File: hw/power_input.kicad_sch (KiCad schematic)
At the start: 8 parts, among them J2 216990-0002, U4 USBLC6-2SC6, U5 TLV70233DSER

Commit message: WIP - nearly all routing complete
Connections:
- net USB_P: now reaches J2.A6 (DP1), J2.B6 (DP2), U4.4
- net USB_N: now reaches J2.A7 (DN1), J2.B7 (DN2), U4.6
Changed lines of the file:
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@@
     (stroke (width 0) (type default))
+  )
+  (label "USB_N" (at 128.27 102.87 0) (fields_autoplaced)
+    (effects (font (size 1.27 1.27)) (justify left bottom))
+  )
+  (label "USB_P" (at 124.46 128.27 0) (fields_autoplaced)
+    (effects (font (size 1.27 1.27)) (justify left bottom))
   )
   (global_label "+3V" (shape input) (at 173.99 54.61 90) (fields_autoplaced)
@@
     (effects (font (size 1.27 1.27)) (justify left))
   )
+  (netclass_flag "" (length 2.54) (shape round) (at 124.46 102.87 0) (fields_autoplaced)
+    (effects (font (size 1.27 1.27)) (justify left bottom))
+    (property "Netclass" "usb" (at 125.0696 100.33 0)
+      (effects (font (size 1.27 1.27) italic) (justify left))
+    )
+  )
+  (netclass_flag "" (length 2.54) (shape round) (at 191.77 113.03 0) (fields_autoplaced)
+    (effects (font (size 1.27 1.27)) (justify left bottom))
+    (property "Netclass" "usb" (at 192.3796 110.49 0)
+      (effects (font (size 1.27 1.27) italic) (justify left))
+    )
+  )
+  (netclass_flag "" (length 2.54) (shape round) (at 134.62 113.03 0) (fields_autoplaced)
+    (effects (font (size 1.27 1.27)) (justify left bottom))
+    (property "Netclass" "usb" (at 135.2296 110.49 0)
+      (effects (font (size 1.27 1.27) italic) (justify left))
+    )
+  )
+  (netclass_flag "" (length 2.54) (shape round) (at 191.77 102.87 0) (fields_autoplaced)
+    (effects (font (size 1.27 1.27)) (justify left bottom))
+    (property "Netclass" "usb" (at 192.3796 100.33 0)
+      (effects (font (size 1.27 1.27) italic) (justify left))
+    )
+  )
   (symbol (lib_id "Device:R_US") (at 34.29 119.38 0) (unit 1)

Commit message: Set up kicadbom and make a pass at filling in all bom entries
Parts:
- J2: MF (none) -> Molex; MPN (none) -> 2169900002
- U4: MF (none) -> ST; MPN (none) -> USBLC6-2SC6
- U5: MF (none) -> TI; MPN (none) -> TLV70233DSER
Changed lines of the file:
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@@
       (effects (font (size 1.27 1.27) italic) hide)
+    )
+    (property "MPN" "2169900002" (at 53.34 101.6 0)
+      (effects (font (size 1.27 1.27)) hide)
+    )
+    (property "MF" "Molex" (at 53.34 101.6 0)
+      (effects (font (size 1.27 1.27)) hide)
     )
     (pin "A1/B12")
@@
       (effects (font (size 1.27 1.27) italic) hide)
     )
+    (property "MPN" "TLV70233DSER" (at 127 66.04 0)
+      (effects (font (size 1.27 1.27)) hide)
+    )
+    (property "MF" "TI" (at 127 66.04 0)
+      (effects (font (size 1.27 1.27)) hide)
+    )
     (pin "1")
     (pin "2")
@@
       (effects (font (size 1.27 1.27) italic) hide)
     )
+    (property "MPN" "USBLC6-2SC6" (at 180.34 102.87 0)
+      (effects (font (size 1.27 1.27)) hide)
+    )
+    (property "MF" "ST" (at 180.34 102.87 0)
+      (effects (font (size 1.27 1.27)) hide)
+    )
     (pin "1")

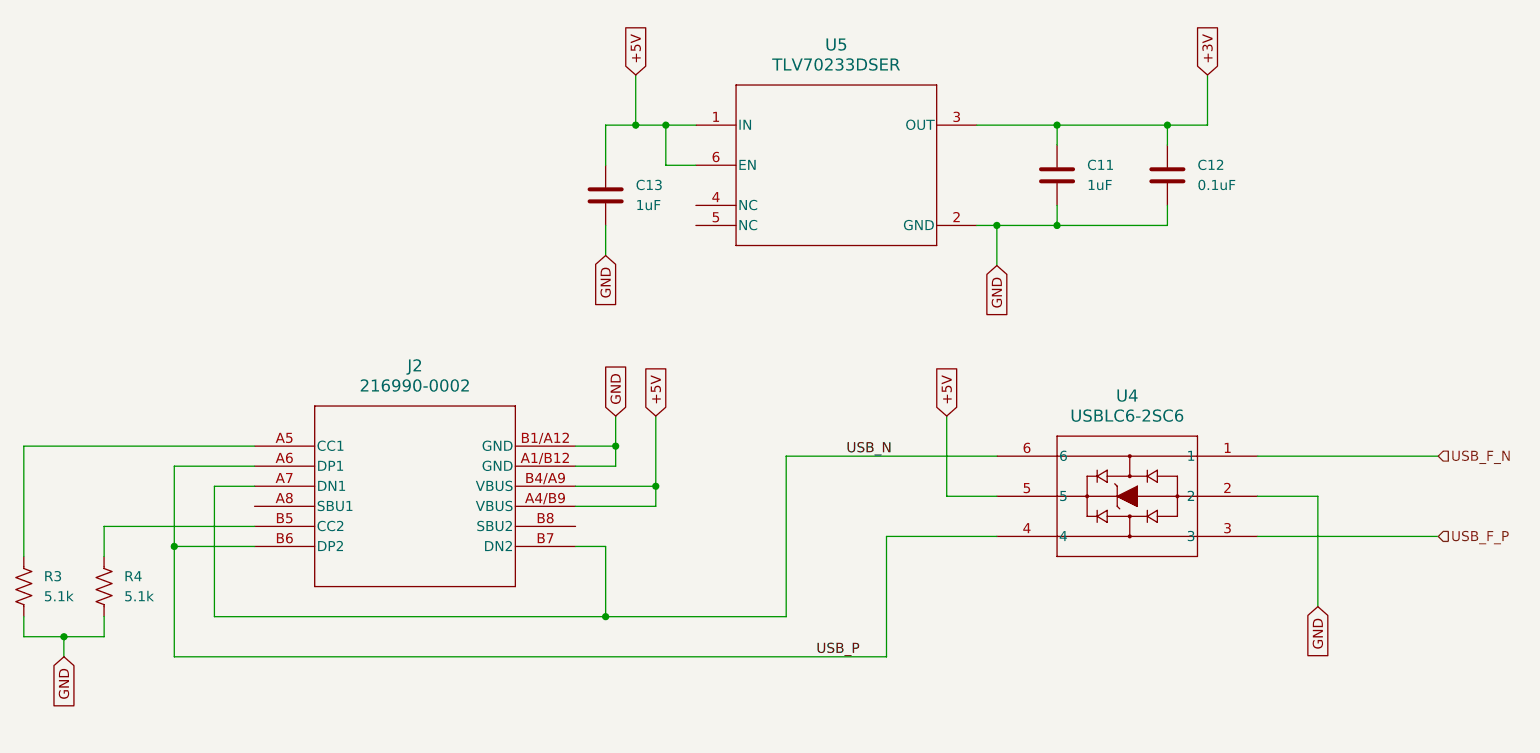
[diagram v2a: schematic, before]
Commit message: r4.1: Swith to an actual SMT USB-C connector
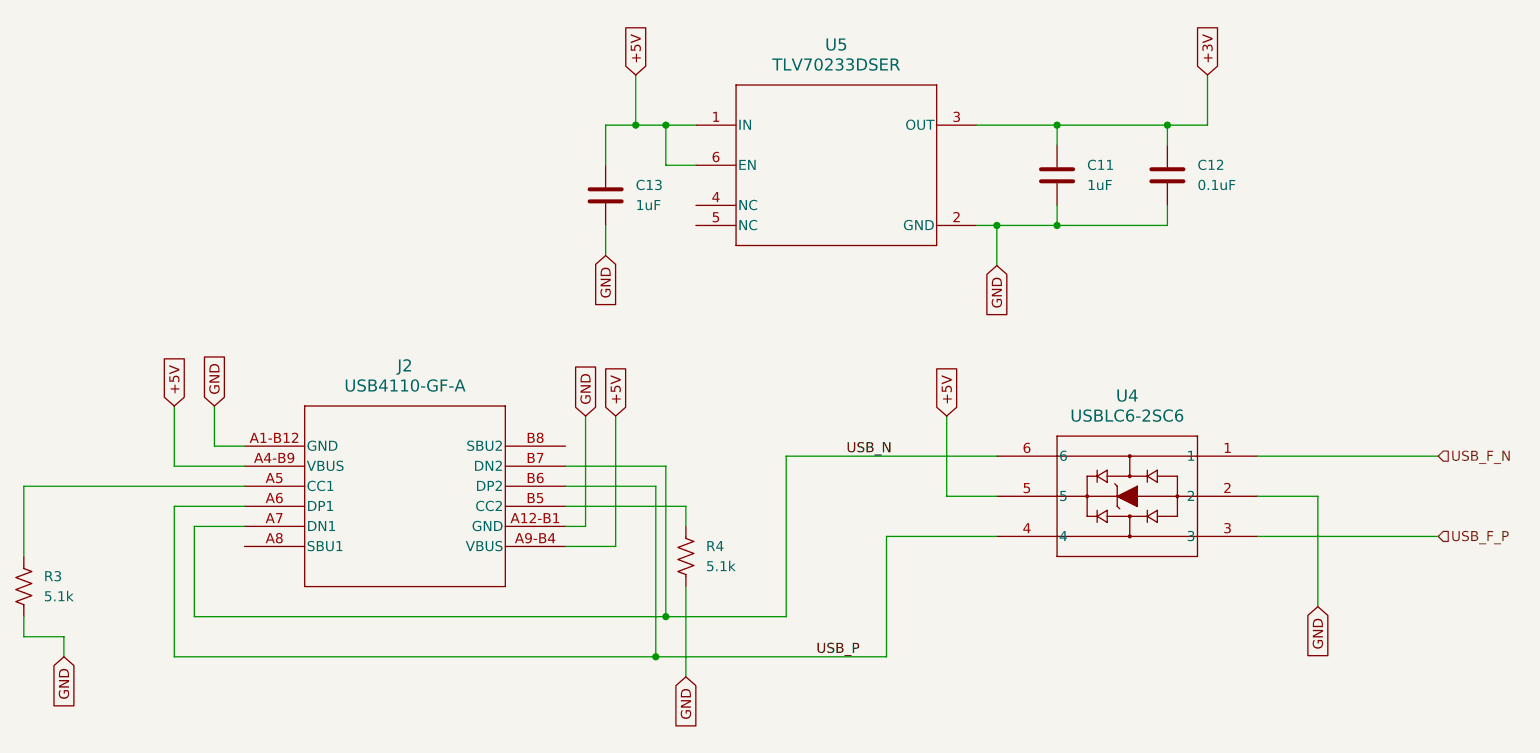
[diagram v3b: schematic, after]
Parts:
- removed J2: 216990-0002, fdcanusb:216990-0002_MOL, symbol fdcanusb:216990-0002
- added J2: USB4110-GF-A, fdcanusb:USB4110-GF-A_GCT, symbol fdcanusb:USB4110-GF-A
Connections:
- net +5V: now also J2.A4-B9 (VBUS), J2.A9-B4 (VBUS)
- net GND: now also J2.A1-B12 (GND), J2.A12-B1 (GND)
- net USB_N: now also J2.A7 (DN1), J2.B7 (DN2)
- net USB_P: now also J2.A6 (DP1), J2.B6 (DP2)
- net at R4.1: now also J2.B5 (CC2)
- net at R3.1: now also J2.A5 (CC1)
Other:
- moved on the sheet: R4

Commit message: Add title block and update rev to r4.2
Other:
- company: (none) -> mjbots Robotic Systems, LLC - info@mjbots.com - 2024
- title: (none) -> mjcanfd-usb-1x r4.2
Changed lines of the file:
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@@
 (kicad_sch (version 20230121) (generator eeschema)
   (paper "A4")
+  (title_block
+    (title "mjcanfd-usb-1x r4.2")
+    (company "mjbots Robotic Systems, LLC - info@mjbots.com - 2024")
+    (comment 1 "Licensed under the Apache 2.0 License")
+  )
   (junction (at 154.94 73.66) (diameter 0) (color 0 0 0 0)
   )
